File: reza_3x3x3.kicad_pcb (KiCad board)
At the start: 2 copper layers, 50 x 50 mm, 20 parts, among them CON1 BARREL_JACK, IC1 ATMEGA88PA-P, K1 CONN_3, K2 CONN_3, P1 CONN_9, P2 CONN_9, P3 DIL6, P4 CONN_2, U1 LP2950

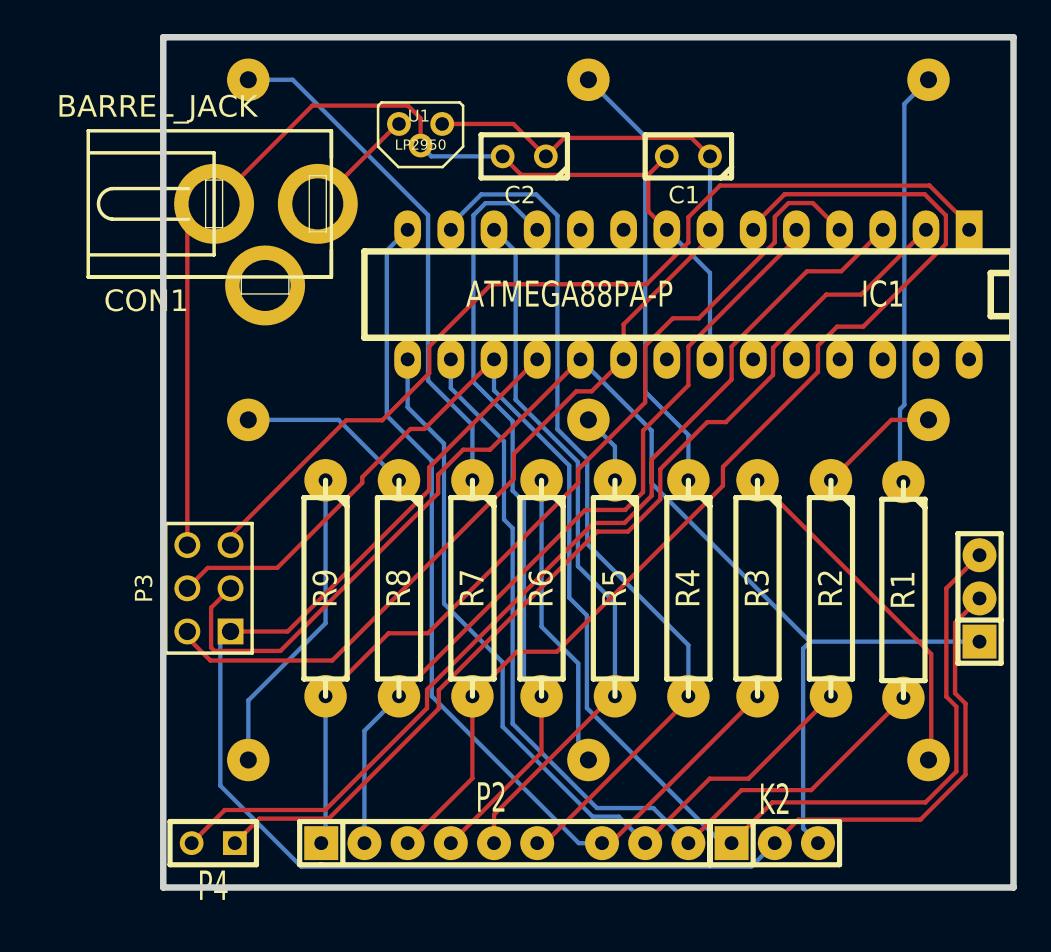
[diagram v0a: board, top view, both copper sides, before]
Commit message: v4 manufacture @ seedstudio
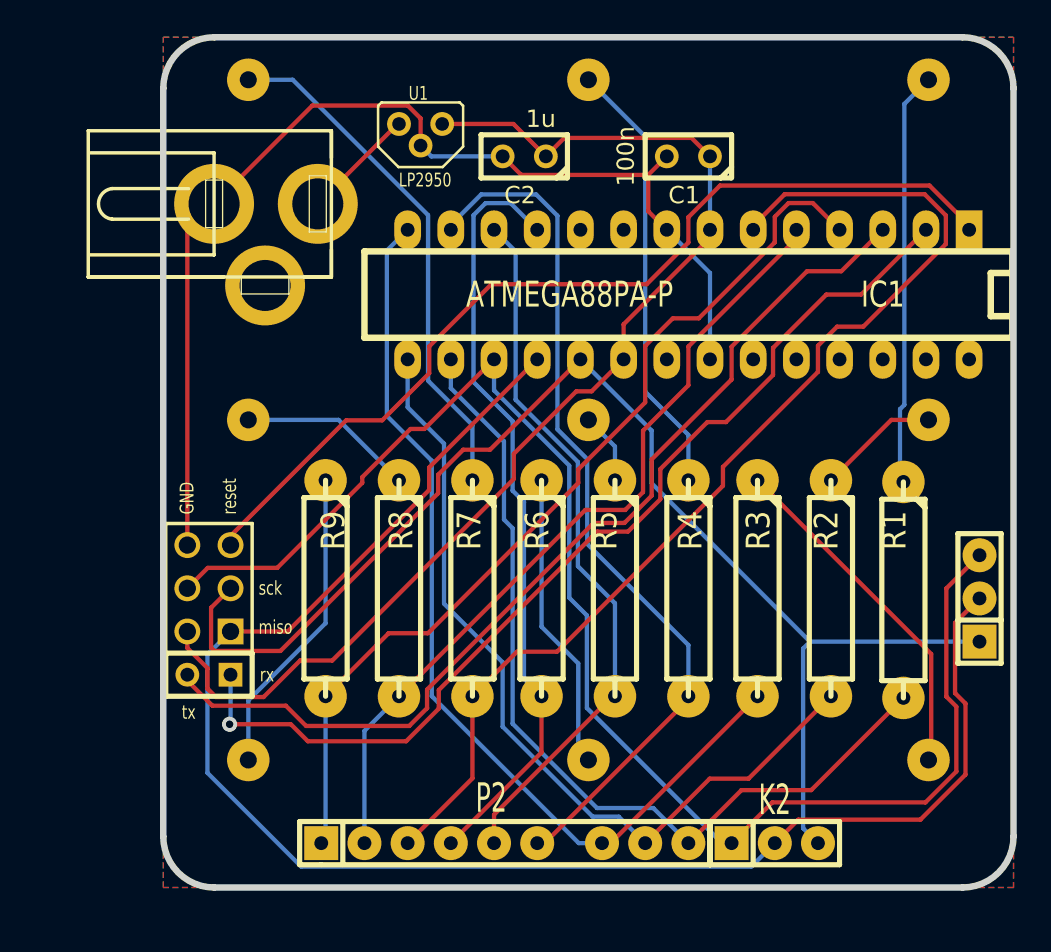
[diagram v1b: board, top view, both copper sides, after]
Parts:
- moved P4 9.91 mm to (27.7, 62.5)
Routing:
- net +5V: track 66.2 -> 69.1 mm
- net /ser_rx: track 58.2 -> 59.4 mm, vias 0 -> 1
- net /ser_tx: track 58.6 -> 57.5 mm
- net /row2: track 94.0 -> 94.6 mm
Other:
- outline, holes or cut-outs redrawn
- board text added: "2014 v4"
- board text added: "GND"
- board text added: "knielsens og asgers led cube kit 3x3x3"
- board text added: "miso"
- board text added: "reset"
- board text added: "rx"
- board text added: "sck"
- board text added: "tx"
